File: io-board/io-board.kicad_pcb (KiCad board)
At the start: 2 copper layers, 82 x 64 mm, 143 parts, among them J1 Conn_01x03, J2 Conn_01x03, J3 Conn_01x03, J4 Conn_01x03, J5 Conn_01x24, K1 FRM18A-5 DC12V, K10 FRM18A-5 DC12V, K11 FRM18A-5 DC12V, K2 FRM18A-5 DC12V, K3 FRM18A-5 DC12V, K4 FRM18A-5 DC12V, K5 FRM18A-5 DC12V, K6 FRM18A-5 DC12V, K7 FRM18A-5 DC12V, K8 FRM18A-5 DC12V, K9 FRM18A-5 DC12V, Q1 NPN, Q10 NPN, Q11 NPN, Q12 NPN, Q13 PNP, Q14 NPN, Q15 PNP, Q16 NPN, Q17 NPN, Q2 NPN, Q3 NPN, Q4 NPN, Q5 NPN, Q6 NPN, Q7 NPN, Q8 NPN, Q9 NPN, U1 Littelfuse SP720, U2 Kamod BluePill STM32F103C8T6

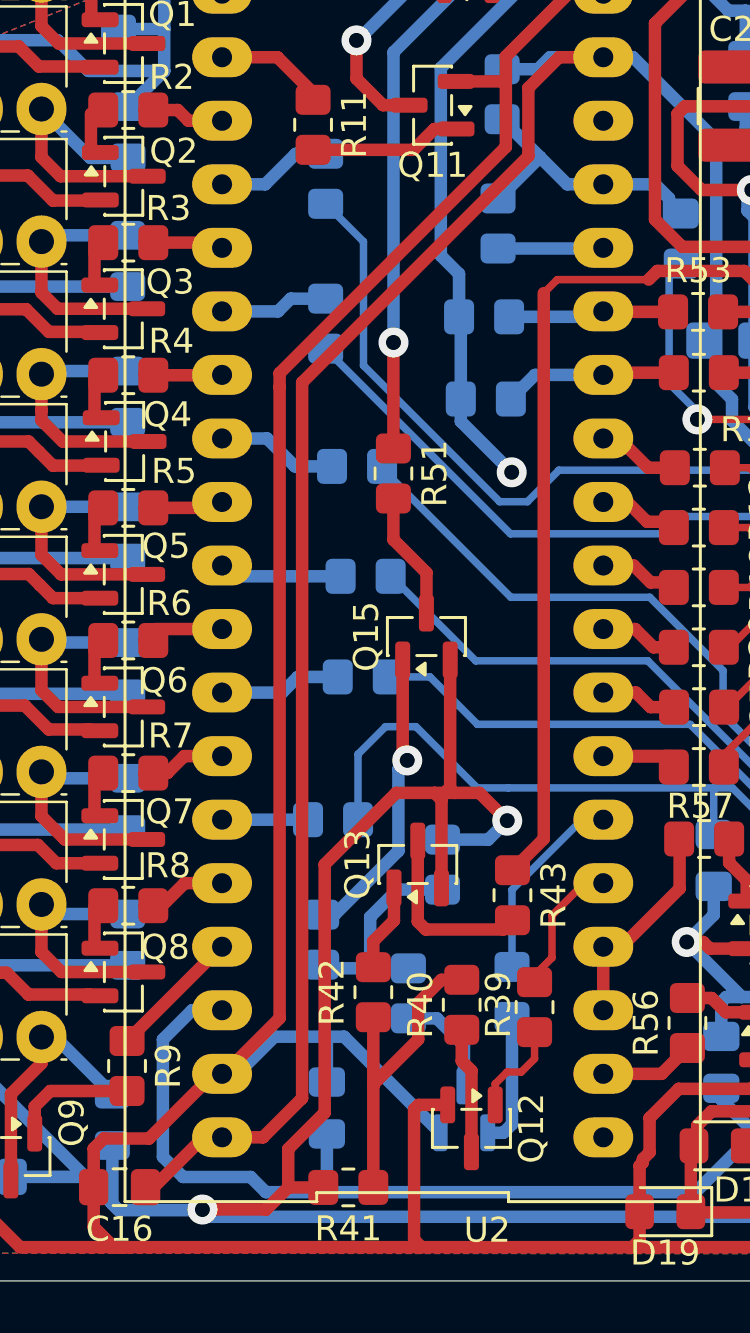
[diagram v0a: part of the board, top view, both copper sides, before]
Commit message: PCB: io: Removed unneeded res in LED driver
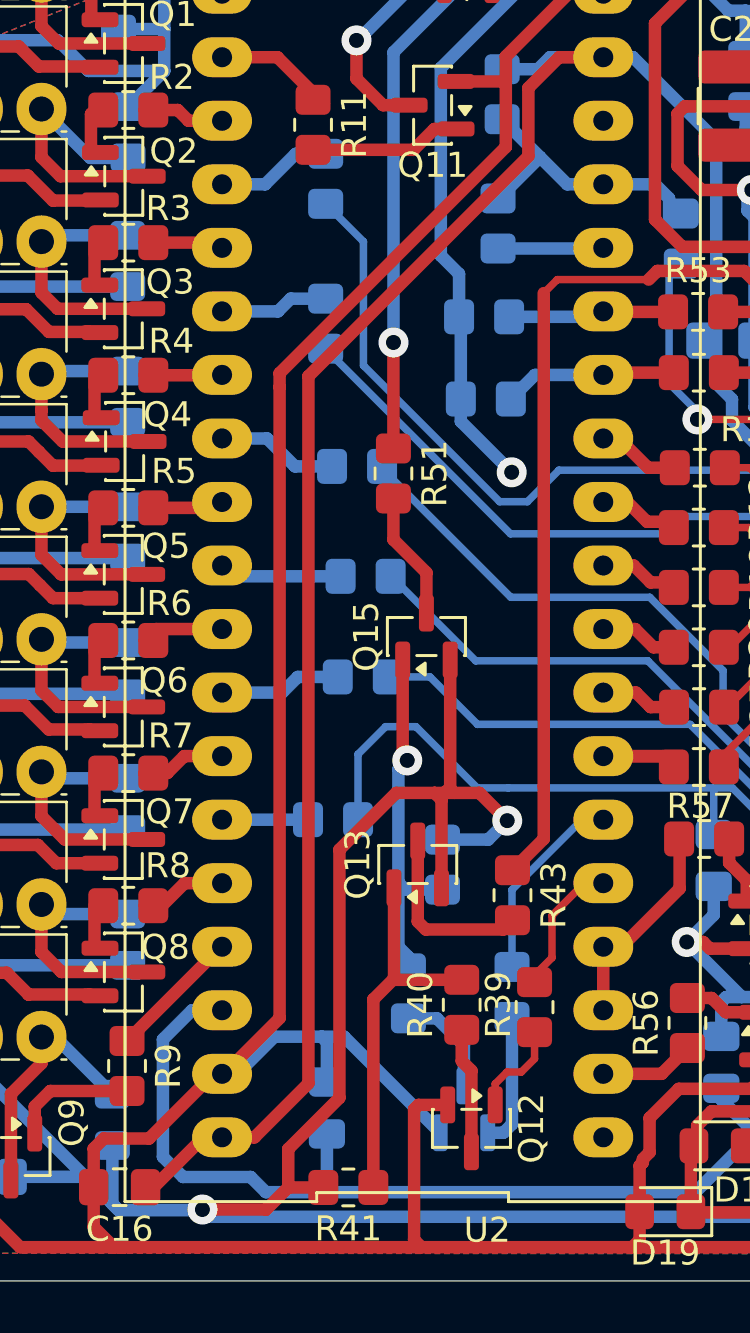
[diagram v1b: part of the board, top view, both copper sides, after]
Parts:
- removed R42, R50: R, Resistor_SMD:R_0805_2012Metric_Pad1.20x1.40mm_HandSolder
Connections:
- R40 pad 2: Net-(R40-Pad2) -> Net-(Q13-B)
- R41 pad 1: Net-(R40-Pad2) -> Net-(Q13-B)
- R48 pad 1: Net-(R48-Pad1) -> Net-(Q15-B)
- R49 pad 2: Net-(R48-Pad1) -> Net-(Q15-B)
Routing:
- net Net-(R40-Pad2): track 13.0 -> 0.00 mm
- net Net-(Q13-B): track 3.51 -> 15.0 mm
- net Net-(R48-Pad1): track 8.92 -> 0.00 mm
- net Net-(Q15-B): track 12.0 -> 14.6 mm
